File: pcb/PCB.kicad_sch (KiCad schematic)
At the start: 28 parts, among them J1 TE 770966-2, J2 TE 770966-2, J3 JST B04B-XASK, K1 AZDC6, Q1 IRLZ44N, U1 LM339, U2 LTV-817S, U3 VRB1205YMD-15WR3

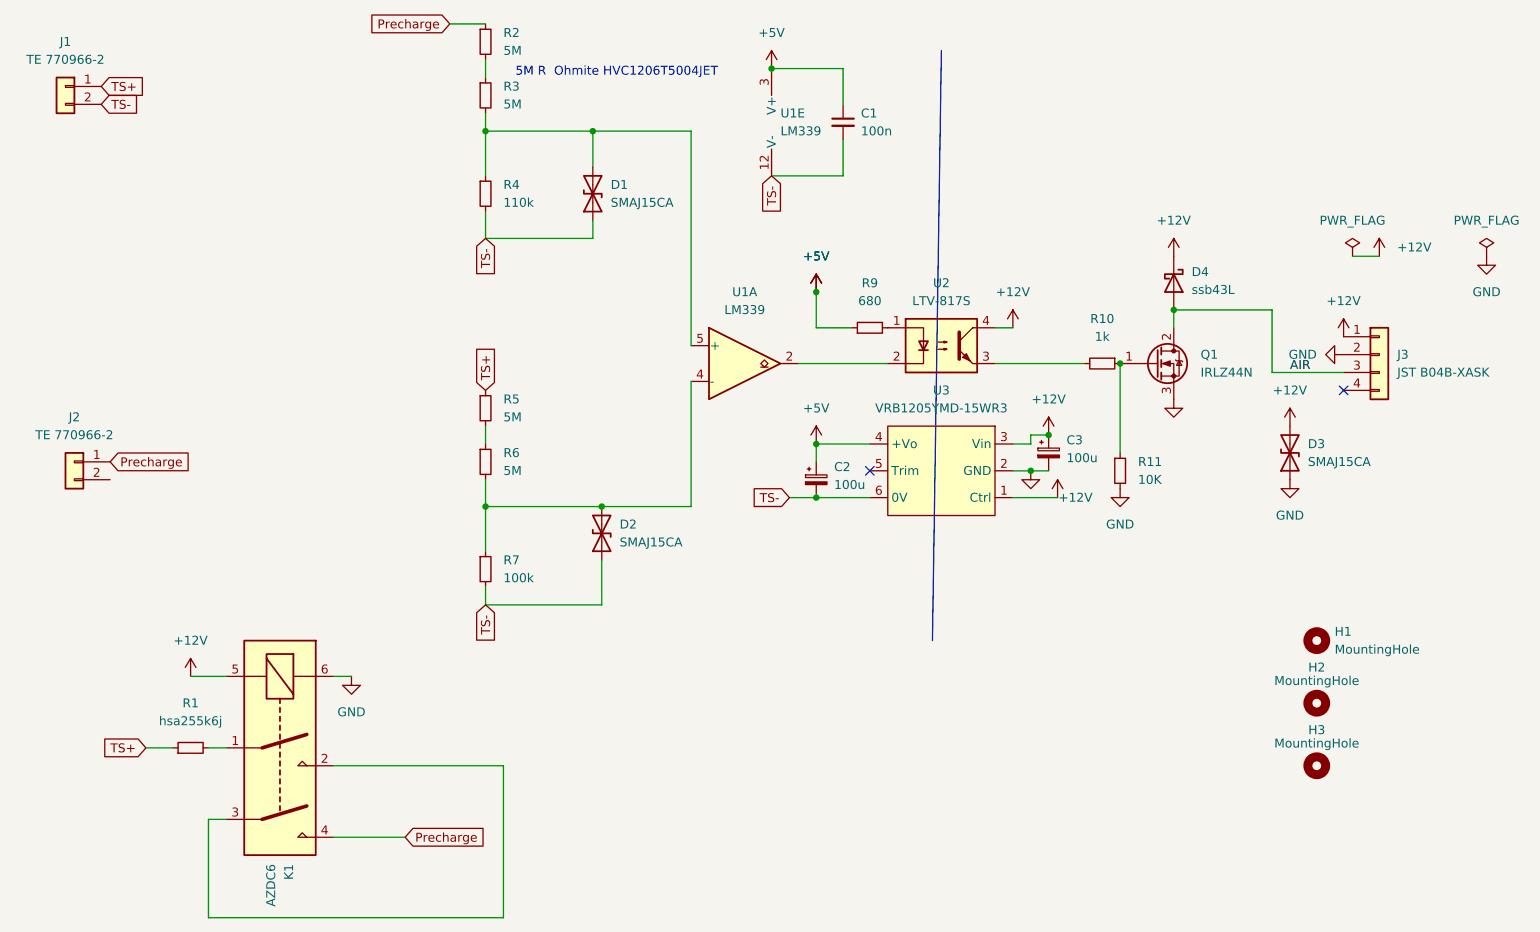
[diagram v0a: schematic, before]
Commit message: Re-layout pcb for br24
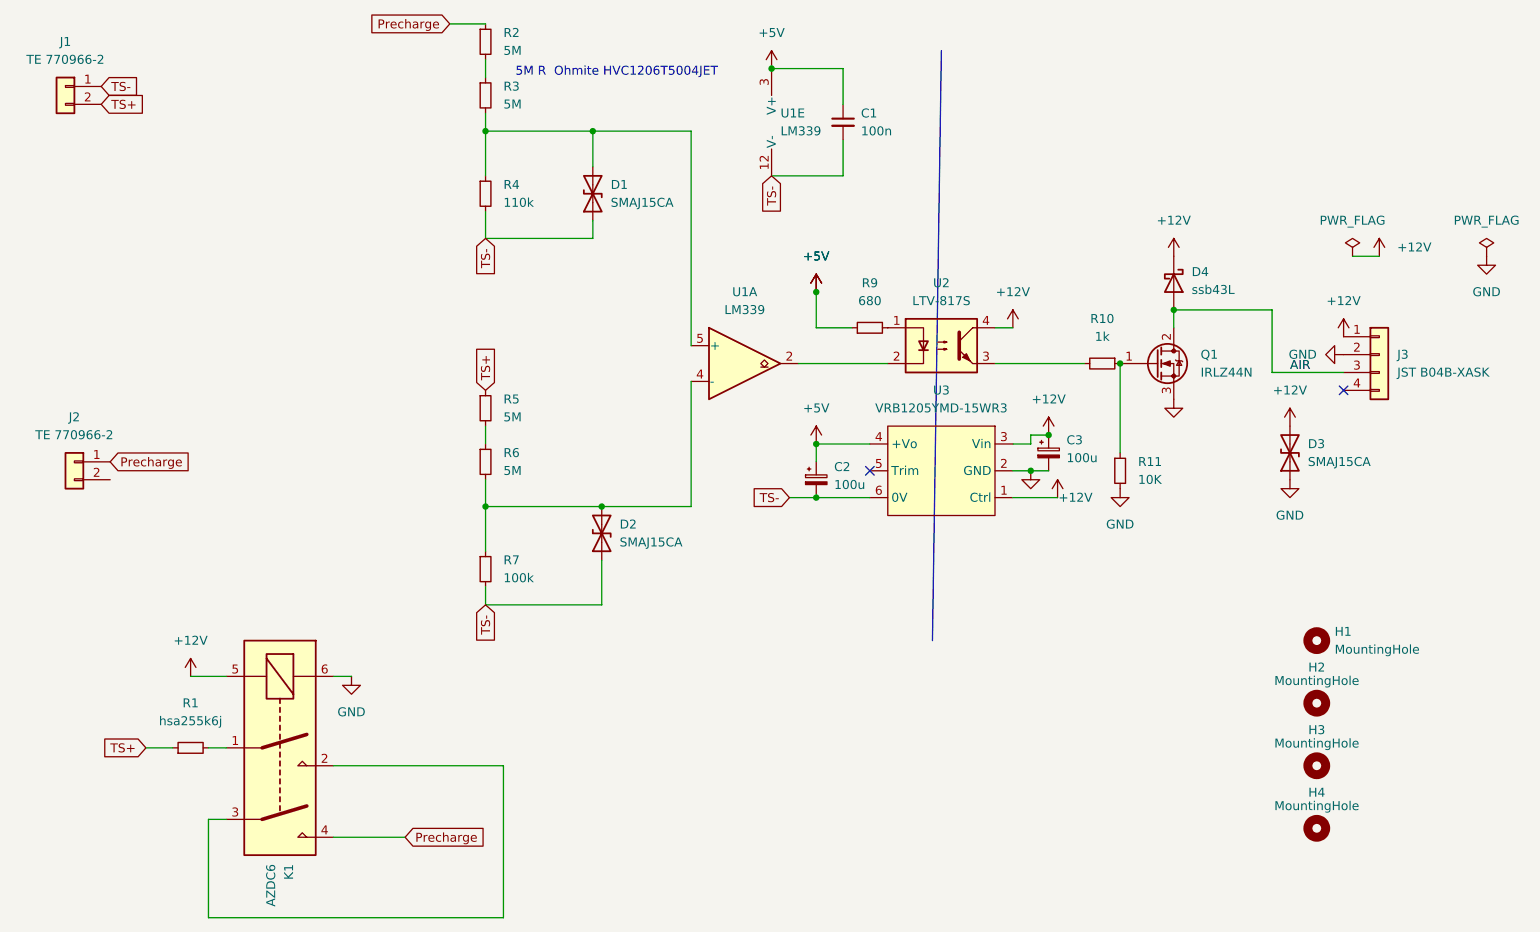
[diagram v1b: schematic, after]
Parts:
- added H4: MountingHole, MountingHole:MountingHole_3.2mm_M3, symbol Mechanical:MountingHole
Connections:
- net TS+: now also J1.2 (Pin_2); no longer J1.1 (Pin_1)
- net TS-: now also J1.1 (Pin_1); no longer J1.2 (Pin_2)
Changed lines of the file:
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@@
     )
   )
-  (global_label "TS+" (shape input) (at 36.83 31.75 0) (fields_autoplaced)
+  (global_label "TS+" (shape input) (at 36.83 34.29 0) (fields_autoplaced)
     (effects (font (size 1.27 1.27)) (justify left))
-    (property "Intersheetrefs" "${INTERSHEET_REFS}" (at 42.9926 31.8294 0)
+    (property "Intersheetrefs" "${INTERSHEET_REFS}" (at 42.9926 34.2106 0)
       (effects (font (size 1.27 1.27)) (justify left) hide)
     )
@@
     )
   )
-  (global_label "TS-" (shape input) (at 36.83 34.29 0) (fields_autoplaced)
+  (global_label "TS-" (shape input) (at 36.83 31.75 0) (fields_autoplaced)
     (effects (font (size 1.27 1.27)) (justify left))
-    (property "Intersheetrefs" "${INTERSHEET_REFS}" (at 42.9926 34.3694 0)
+    (property "Intersheetrefs" "${INTERSHEET_REFS}" (at 42.9926 31.6706 0)
       (effects (font (size 1.27 1.27)) (justify left) hide)
     )
@@
         )
       )
+    )
+  )
+  (symbol (lib_id "Mechanical:MountingHole") (at 209.55 137.16 0) (unit 1)
+    (in_bom yes) (on_board yes) (dnp no)
+    (property "Reference" "H4" (at 209.55 132.08 0)
+      (effects (font (size 1.27 1.27)))
+    )
+    (property "Value" "MountingHole" (at 209.55 133.985 0)
+      (effects (font (size 1.27 1.27)))
+    )
+    (property "Footprint" "MountingHole:MountingHole_3.2mm_M3" (at 209.55 137.16 0)
+      (effects (font (size 1.27 1.27)) hide)
+    )
+    (property "Datasheet" "~" (at 209.55 137.16 0)
+      (effects (font (size 1.27 1.27)) hide)
+    )
+    (instances
+      (project "PCB"
+        (path "/68f34db6-b185-48e2-8817-fb07f7d1240e"
+          (reference "H4") (unit 1)
+        )
+      )

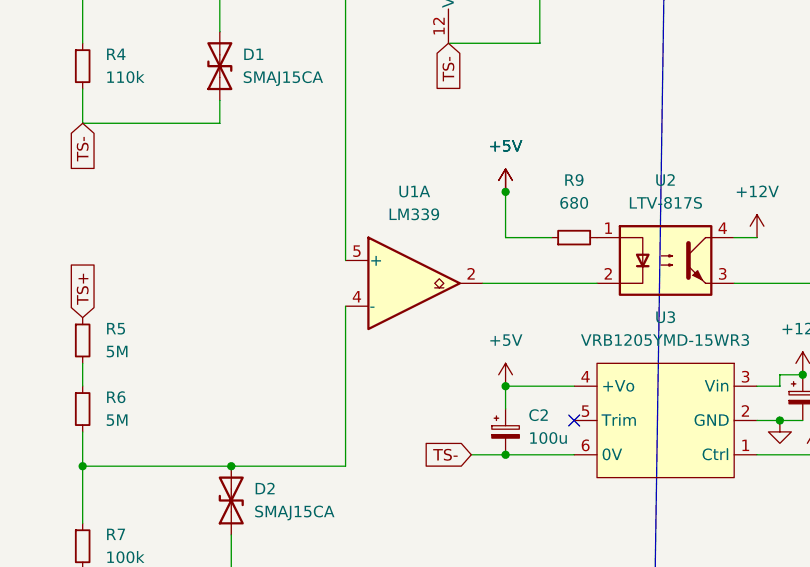
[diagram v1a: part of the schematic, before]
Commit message: fix backwards comparator
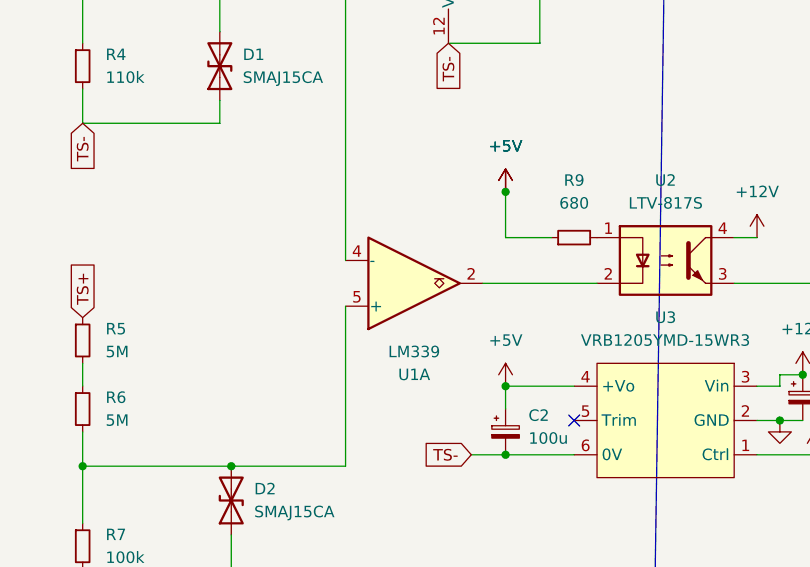
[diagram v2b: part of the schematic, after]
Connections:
- net at D2.2 (A2), R6.2, R7.1: now also U1.5 (+); no longer U1.4 (-)
- net at D1.2 (A2), R3.2, R4.1: now also U1.4 (-); no longer U1.5 (+)
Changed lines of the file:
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@@
     )
   )
-  (symbol (lib_id "Comparator:LM339") (at 128.27 71.12 0) (unit 1)
-    (in_bom yes) (on_board yes) (dnp no) (fields_autoplaced)
-    (property "Reference" "U1" (at 128.27 60.96 0)
+  (symbol (lib_id "Comparator:LM339") (at 128.27 71.12 0) (mirror x) (unit 1)
+    (in_bom yes) (on_board yes) (dnp no)
+    (property "Reference" "U1" (at 128.27 81.28 0)
       (effects (font (size 1.27 1.27)))
     )
-    (property "Value" "LM339" (at 128.27 63.5 0)
+    (property "Value" "LM339" (at 128.27 78.74 0)
       (effects (font (size 1.27 1.27)))
     )
-    (property "Footprint" "Package_SO:TSSOP-14_4.4x5mm_P0.65mm" (at 127 68.58 0)
+    (property "Footprint" "Package_SO:TSSOP-14_4.4x5mm_P0.65mm" (at 127 73.66 0)
       (effects (font (size 1.27 1.27)) hide)
     )
-    (property "Datasheet" "https://www.st.com/resource/en/datasheet/lm139.pdf" (at 129.54 66.04 0)
+    (property "Datasheet" "https://www.st.com/resource/en/datasheet/lm139.pdf" (at 129.54 76.2 0)
       (effects (font (size 1.27 1.27)) hide)
     )
